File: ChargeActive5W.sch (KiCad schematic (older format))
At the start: 34 parts, among them Q2 IRLB3813PbF, Q3 IRLB3813PbF, U28 LM358

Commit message: Placement première charge active
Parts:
- renumbered TPV+1 to V+1, TPV+2 to V+2, TPV-1 to V-1, TPV-2 to V-2, TPVAD1 to VAD1, TPVAD2 to VAD2, TPVGS1 to VGS1, TPVGS2 to VGS2

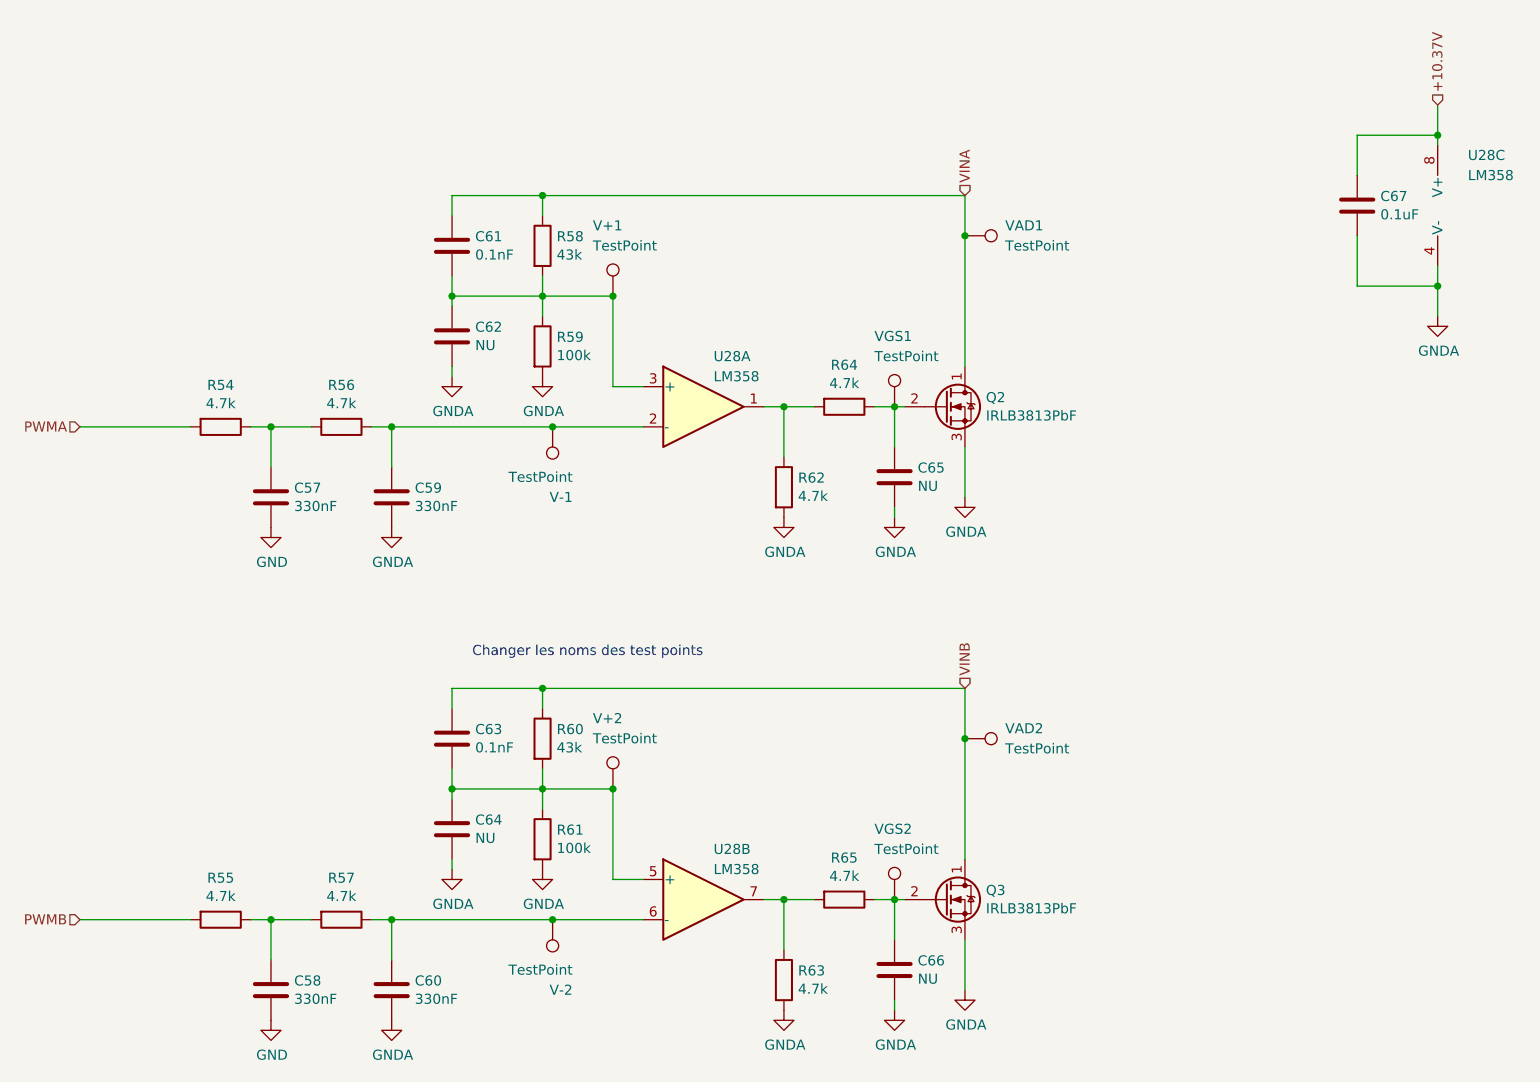
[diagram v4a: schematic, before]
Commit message: Petit ajustement pour accomoder le usb du arduino, pret pour routing
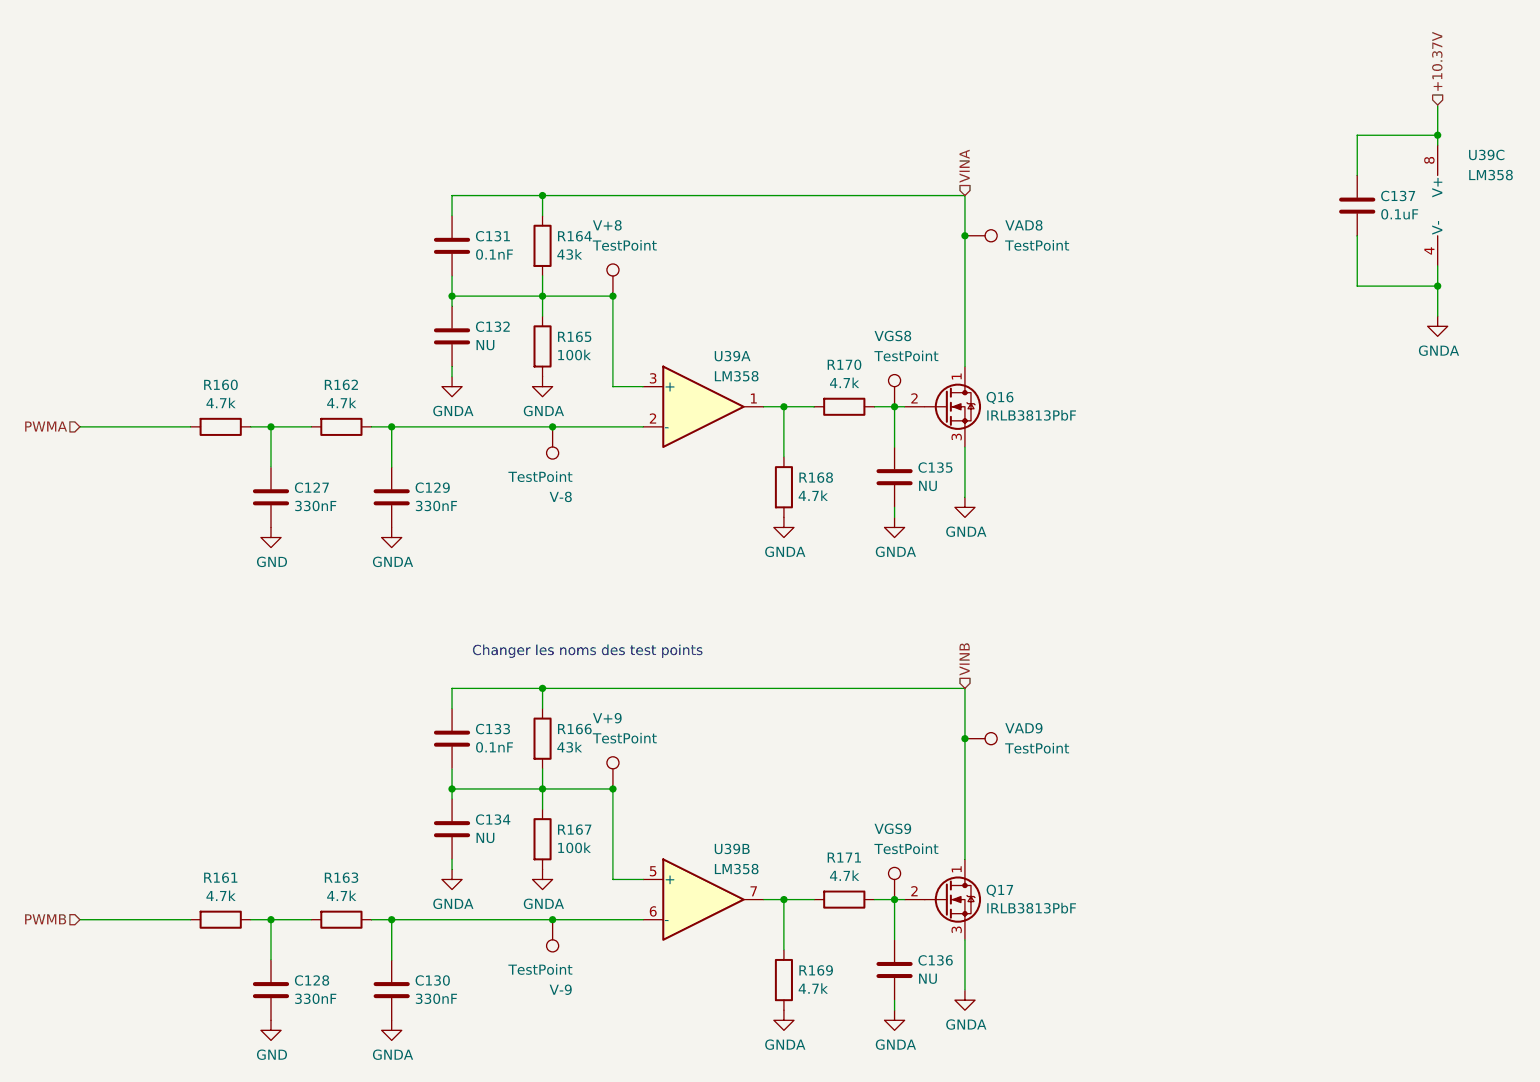
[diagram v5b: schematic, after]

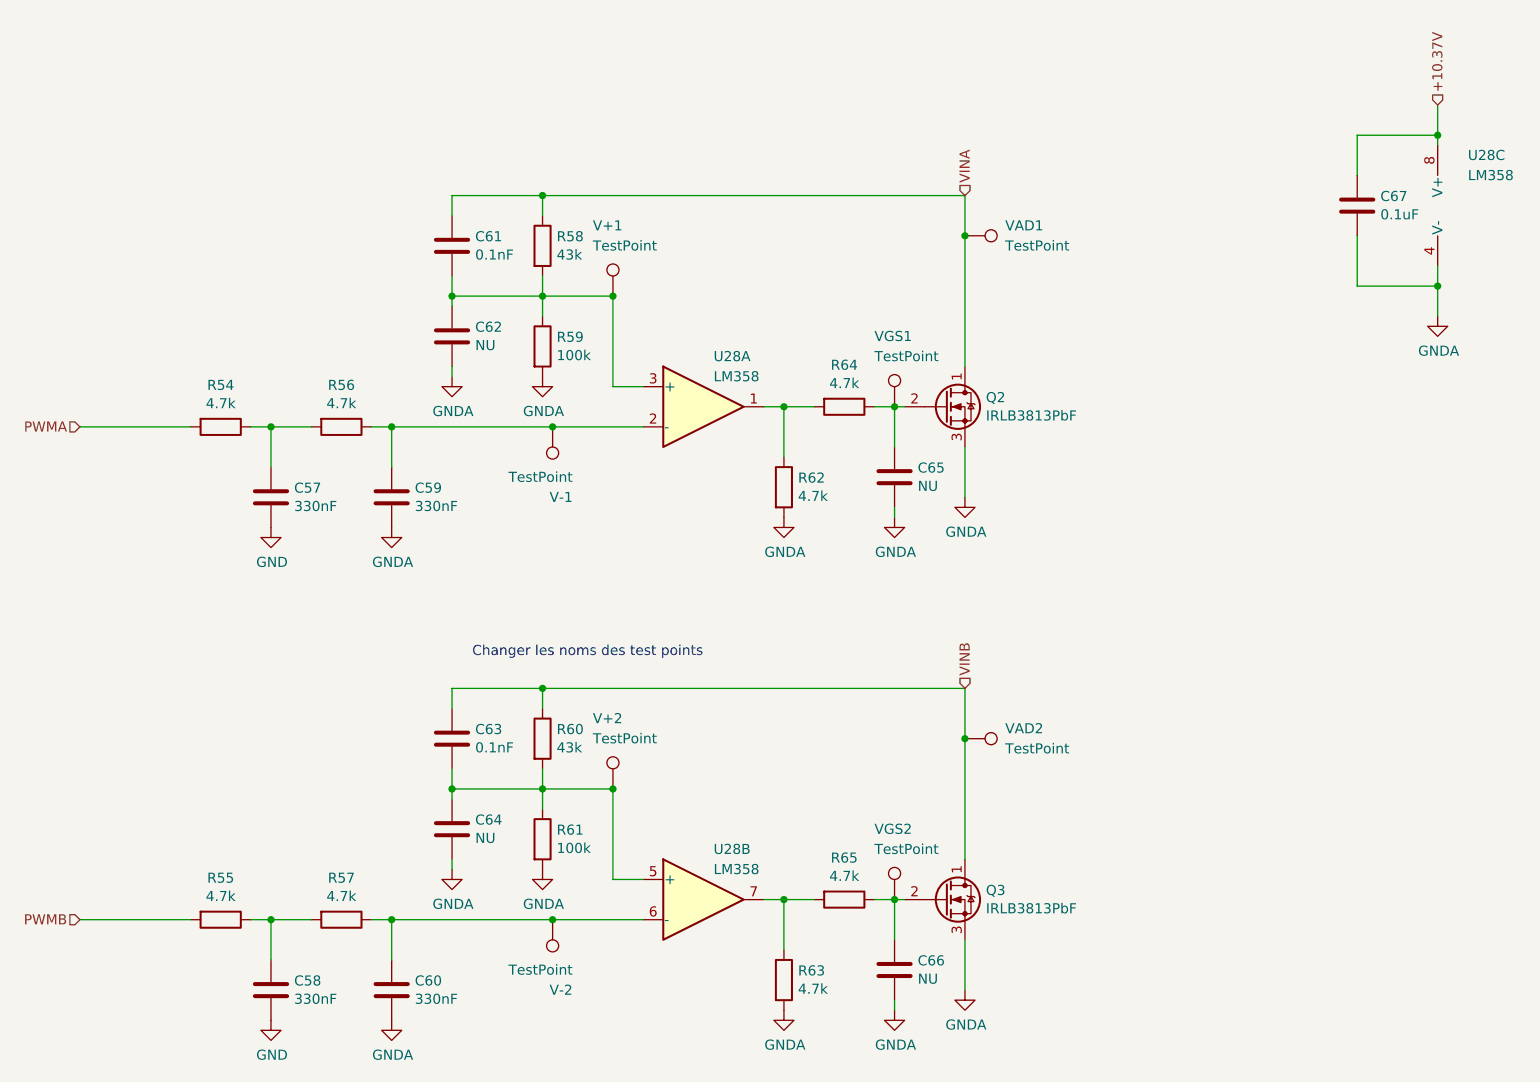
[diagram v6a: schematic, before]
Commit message: retrait des test points inutiles
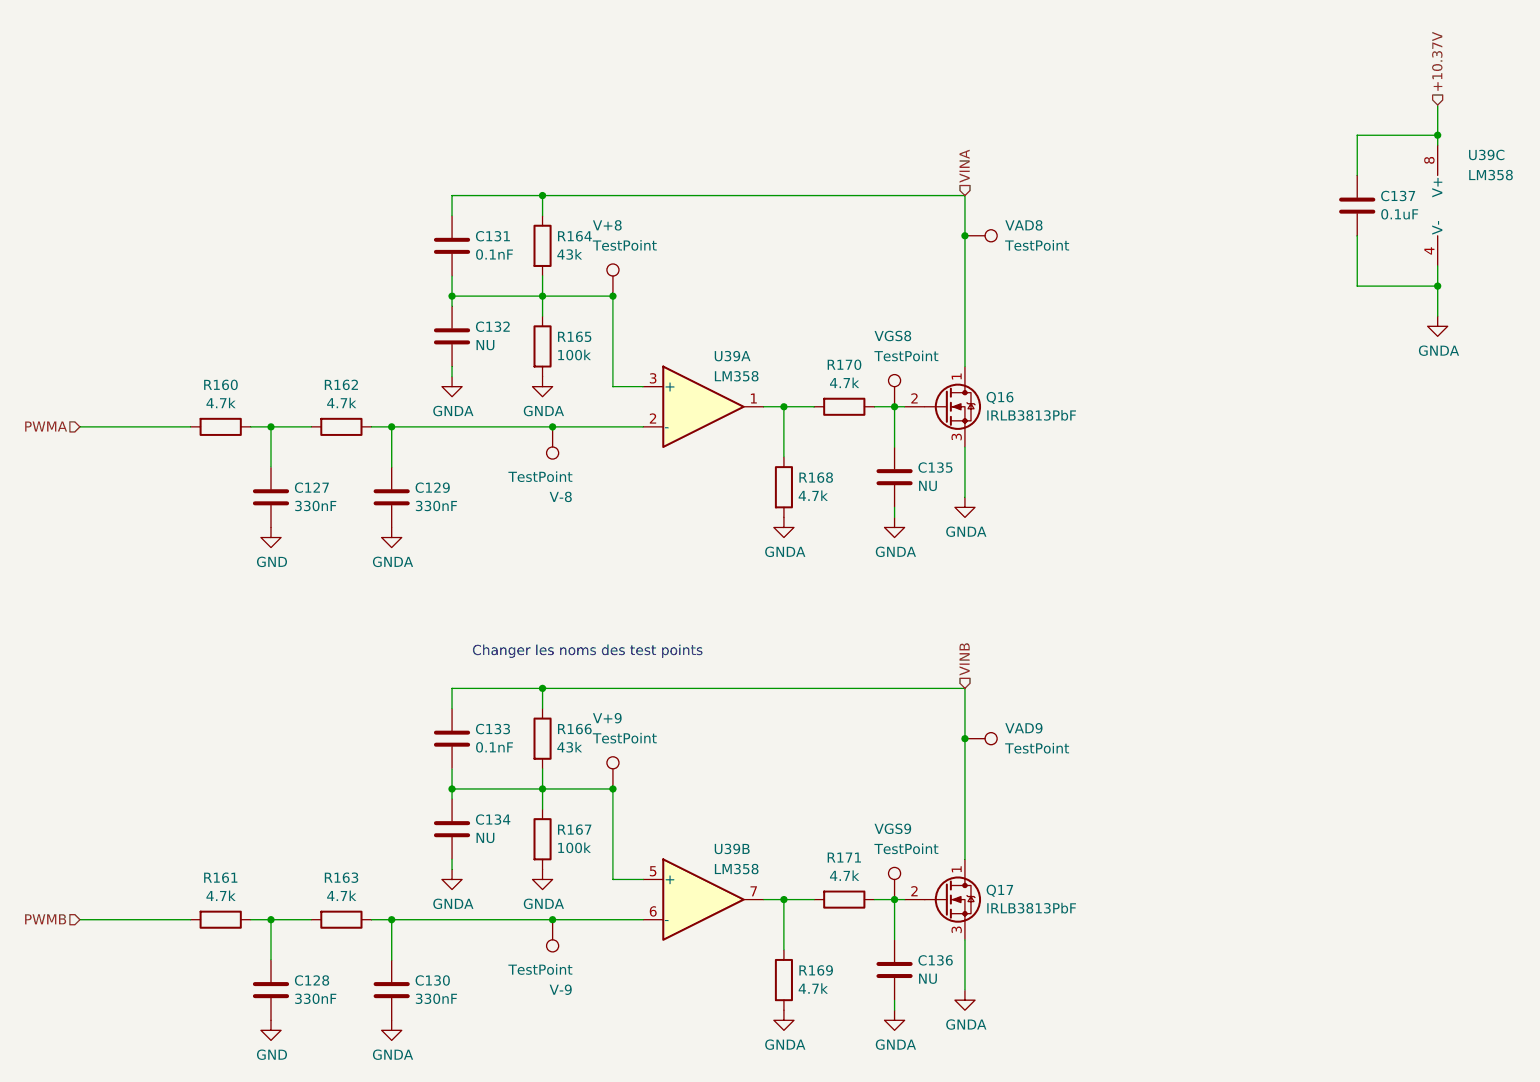
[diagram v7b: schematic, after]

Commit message: Routed most of the power
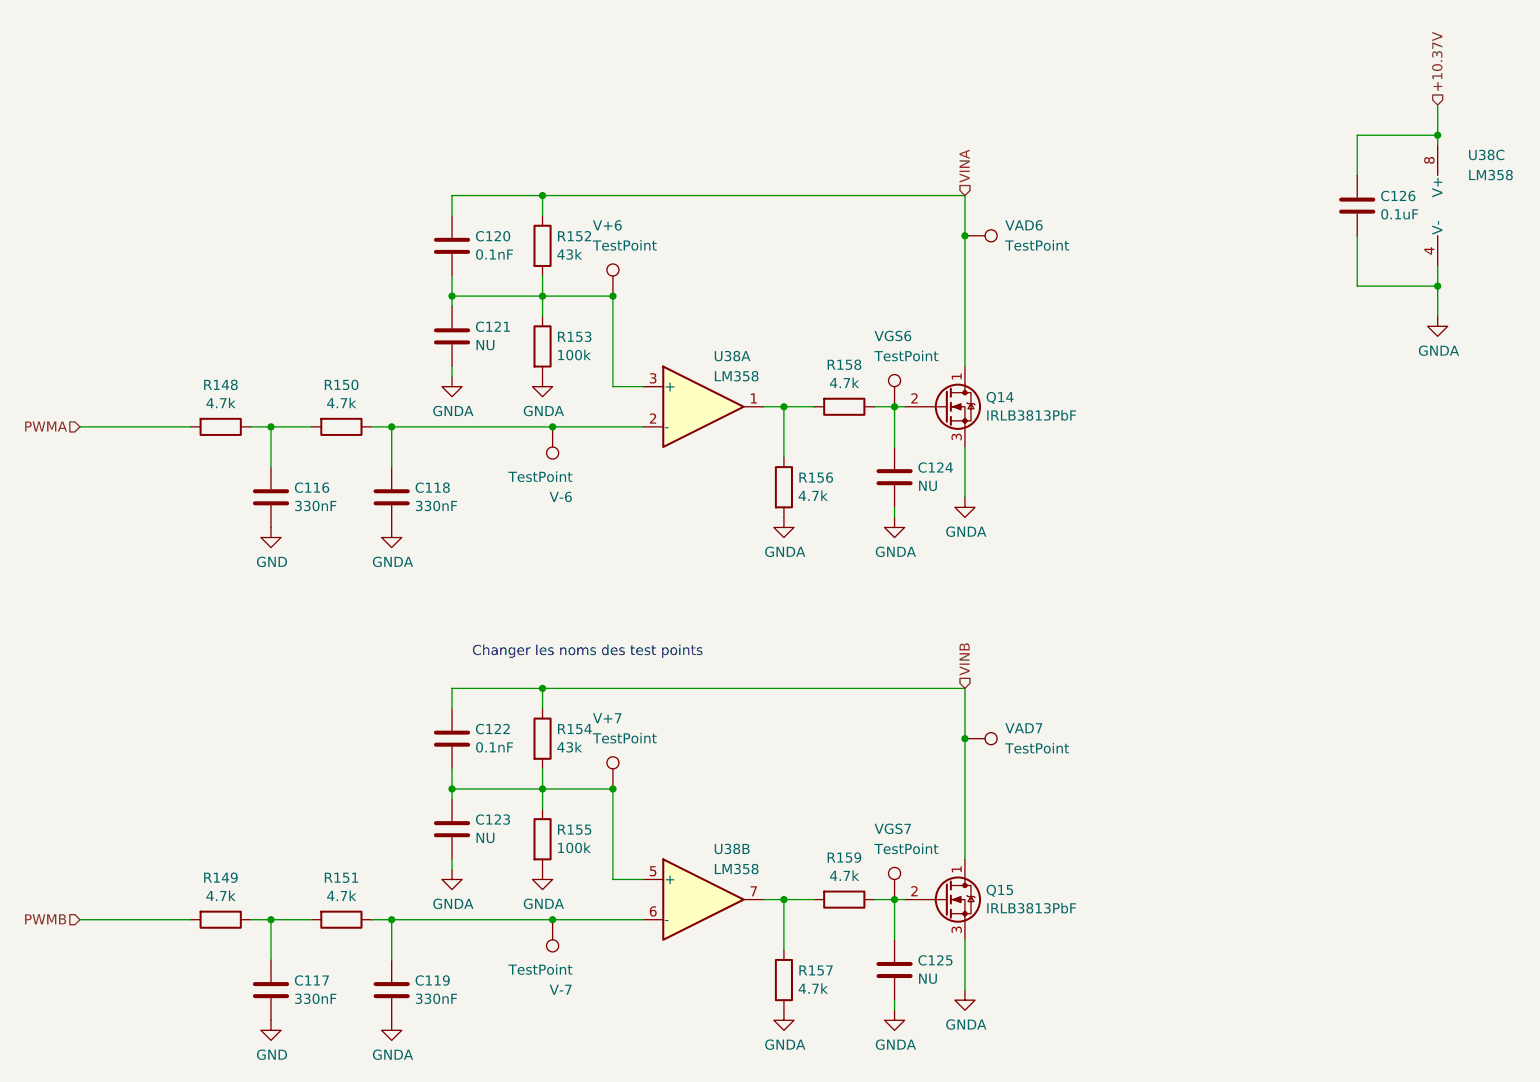
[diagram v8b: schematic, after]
